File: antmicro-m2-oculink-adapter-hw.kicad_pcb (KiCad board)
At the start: 4 copper layers, 22 x 80 mm, 24 parts, among them J1 PCB-Edge_M.2_Key-M, J2 OCuLink_x4_Amphenol_G14A42121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

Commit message: [#81131] Clean drc
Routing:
- net /~{PERST}: track 58.2 -> 60.8 mm
- added copper zone on F.Cu, net Net-(J2-V_{ACT}_TX_3V3)
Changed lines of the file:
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@@
 		(tags "resistor SMD 0201")
 		(property "Reference" "R6"
-			(at 0.26 0.32 180)
+			(at -3.95 -0.85 180)
 			(layer "B.SilkS")
 			(effects
@@
 		(tags "resistor SMD 0201")
 		(property "Reference" "R9"
-			(at 1.03 -0.35 90)
+			(at 1 -0.39 90)
 			(layer "B.SilkS")
 			(effects
@@
 		(tags "resistor SMD 0201")
 		(property "Reference" "R4"
-			(at 0.25 -3.62 180)
+			(at -3.95 -1.44 180)
 			(layer "B.SilkS")
 			(effects
@@
 		(tags "resistor SMD 0201")
 		(property "Reference" "R3"
-			(at 0.5 -3.57 180)
+			(at -3.7 -1.39 180)
 			(layer "B.SilkS")
 			(effects
@@
 		(tags "resistor SMD 0201")
 		(property "Reference" "R2"
-			(at 0.7 -4.38 0)
+			(at 0.88 -4.45 0)
 			(layer "B.SilkS")
 			(effects
@@
 		(tags "resistor SMD 0201")
 		(property "Reference" "R5"
-			(at 0.5 0.35 0)
+			(at -3.71 -0.82 0)
 			(layer "B.SilkS")
 			(effects
@@
 	)
 	(segment
+		(start 147.89 97.424644)
+		(end 147.816435 97.498209)
+		(width 0.25)
+		(layer "F.Cu")
+		(net 1)
+	)
+	(segment
 		(start 138.34 122.22)
 		(end 137.74 122.22)
@@
 	)
 	(segment
-		(start 147.77 97.61)
-		(end 147.77 97.63)
-		(width 0.25)
-		(layer "F.Cu")
-		(net 1)
-	)
-	(segment
-		(start 147.767041 96.797041)
-		(end 147.77 96.8)
-		(width 0.25)
-		(layer "F.Cu")
-		(net 1)
-	)
-	(segment
 		(start 138.34 122.22)
 		(end 138.34 122.3)
@@
 	)
 	(segment
+		(start 147.767041 96.797041)
+		(end 147.89 96.92)
+		(width 0.25)
+		(layer "F.Cu")
+		(net 1)
+	)
+	(segment
 		(start 153.35 127.038482)
 		(end 153.4 127.088482)
@@
 	)
 	(segment
+		(start 147.89 96.92)
+		(end 147.89 97.424644)
+		(width 0.25)
+		(layer "F.Cu")
+		(net 1)
+	)
+	(segment
 		(start 144.27 93.713732)
 		(end 144.278134 93.721866)
@@
 	)
 	(segment
-		(start 147.77 97.462296)
-		(end 147.77 96.8)
-		(width 0.25)
-		(layer "F.Cu")
-		(net 1)
-	)
-	(segment
 		(start 145.91 127.056898)
 		(end 145.9 127.066898)
@@
 	)
 	(via
-		(at 147.77 97.61)
+		(at 147.816435 97.498209)
 		(size 0.5)
 		(drill 0.2)
@@
 	(segment
 		(start 144.51 92.75)
-		(end 144.33 92.57)
+		(end 144.36 92.75)
 		(width 0.2)
 		(layer "F.Cu")
@@
 	)
 	(segment
-		(start 144.18 92.57)
-		(end 142.7 91.09)
+		(start 142.7 91.09)
+		(end 142.7 90.34)
 		(width 0.2)
 		(layer "F.Cu")
@@
 	)
 	(segment
-		(start 142.7 91.09)
-		(end 142.7 90.34)
+		(start 142.02 89.66)
+		(end 140.75 89.66)
 		(width 0.2)
 		(layer "F.Cu")
@@
 	)
 	(segment
-		(start 144.33 92.57)
-		(end 144.18 92.57)
+		(start 144.36 92.75)
+		(end 142.7 91.09)
 		(width 0.2)
 		(layer "F.Cu")
@@
 		(net 24)
 	)
-	(segment
-		(start 142.02 89.66)
-		(end 140.75 89.66)
-		(width 0.2)
-		(layer "F.Cu")
-		(net 24)
-	)
 	(via
 		(at 145.70541 97.737935)
@@
 	)
 	(segment
-		(start 144.51 92.75)
-		(end 144.67 92.75)
-		(width 0.2)
-		(layer "B.Cu")
-		(net 24)
-	)
-	(segment
 		(start 144.71 94.44)
 		(end 144.71 95.71)
@@
 	)
 	(segment
-		(start 144.82 93.772013)
-		(end 144.71 93.882013)
+		(start 144.747 94.403)
+		(end 144.71 94.44)
 		(width 0.2)
 		(layer "B.Cu")
@@
 	)
 	(segment
-		(start 144.82 92.9)
-		(end 144.82 93.772013)
+		(start 145.732065 97.737935)
+		(end 145.70541 97.737935)
 		(width 0.2)
 		(layer "B.Cu")
@@
 	)
 	(segment
-		(start 145.732065 97.737935)
-		(end 145.70541 97.737935)
+		(start 144.51 92.75)
+		(end 144.67 92.75)
 		(width 0.2)
 		(layer "B.Cu")
@@
 	(segment
 		(start 144.67 92.75)
-		(end 144.82 92.9)
+		(end 144.747 92.827)
 		(width 0.2)
 		(layer "B.Cu")
@@
 	)
 	(segment
-		(start 144.71 93.882013)
+		(start 144.7 94.43)
 		(end 144.71 94.44)
 		(width 0.2)
@@
 	)
 	(segment
-		(start 144.7 94.43)
-		(end 144.71 94.44)
+		(start 145.74 96.74)
+		(end 145.74 97.73)
 		(width 0.2)
 		(layer "B.Cu")
@@
 	)
 	(segment
-		(start 145.74 96.74)
-		(end 145.74 97.73)
+		(start 144.747 92.827)
+		(end 144.747 94.403)
 		(width 0.2)
 		(layer "B.Cu")
@@
 	)
 	(segment
+		(start 145.27 95.37)
+		(end 145.124 95.224)
+		(width 0.2)
+		(layer "B.Cu")
+		(net 55)
+	)
+	(segment
 		(start 139.7 118.16)
 		(end 139.07 118.79)
@@
 	)
 	(segment
+		(start 145.124 95.224)
+		(end 145.124 93.130106)
+		(width 0.2)
+		(layer "B.Cu")
+		(net 55)
+	)
+	(segment
+		(start 145.124 93.130106)
+		(end 145.353999 92.900107)
+		(width 0.2)
+		(layer "B.Cu")
+		(net 55)
+	)
+	(segment
 		(start 145.353999 92.900107)
 		(end 145.336946 92.900107)
@@
 	)
 	(zone
-		(net 17)
-		(net_name "+3V3")
+		(net 57)
+		(net_name "Net-(J2-V_{ACT}_TX_3V3)")
 		(layer "F.Cu")
 		(hatch edge 0.5)
@@
 		(members "06556173-ffed-4031-9924-a6c8c4b07c0c" "16721270-387f-447d-a762-376c3936303d")
 	)
-	(group ""
-		(members "477021a0-9647-45d7-a17e-5ebdb906f6e6" "7ca616a6-a283-4b4f-b5f9-dcc5ec1ff0d3"
-			"8a60c2c5-ed15-4a37-9b29-e375b5fa27e6" "fdb1dcc9-0d94-4d31-af9d-c221d9242106"
-			"fe71ac52-9aba-4c5f-a7bf-c88477ec28cb"
-		)
-	)
 	(generated

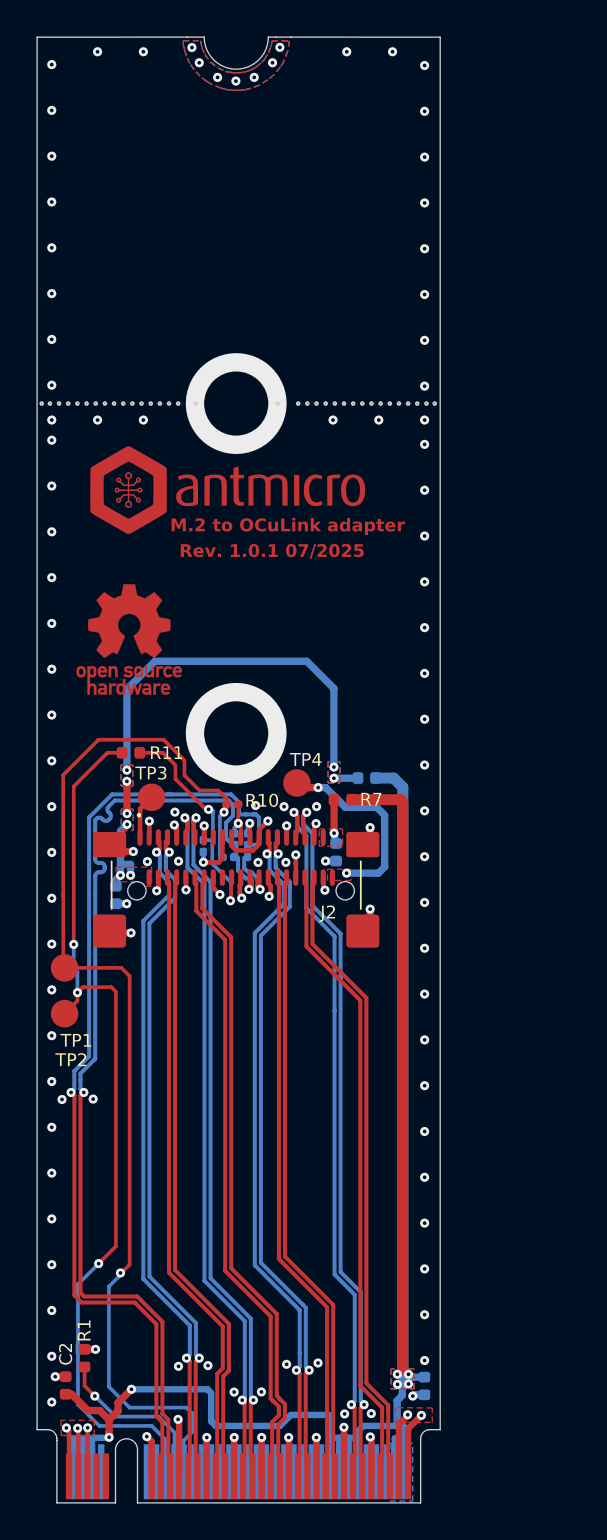
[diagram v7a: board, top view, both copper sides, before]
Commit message: [#81131] Clean-up tracks, shorten stubs, relocate R1, align silkscreen
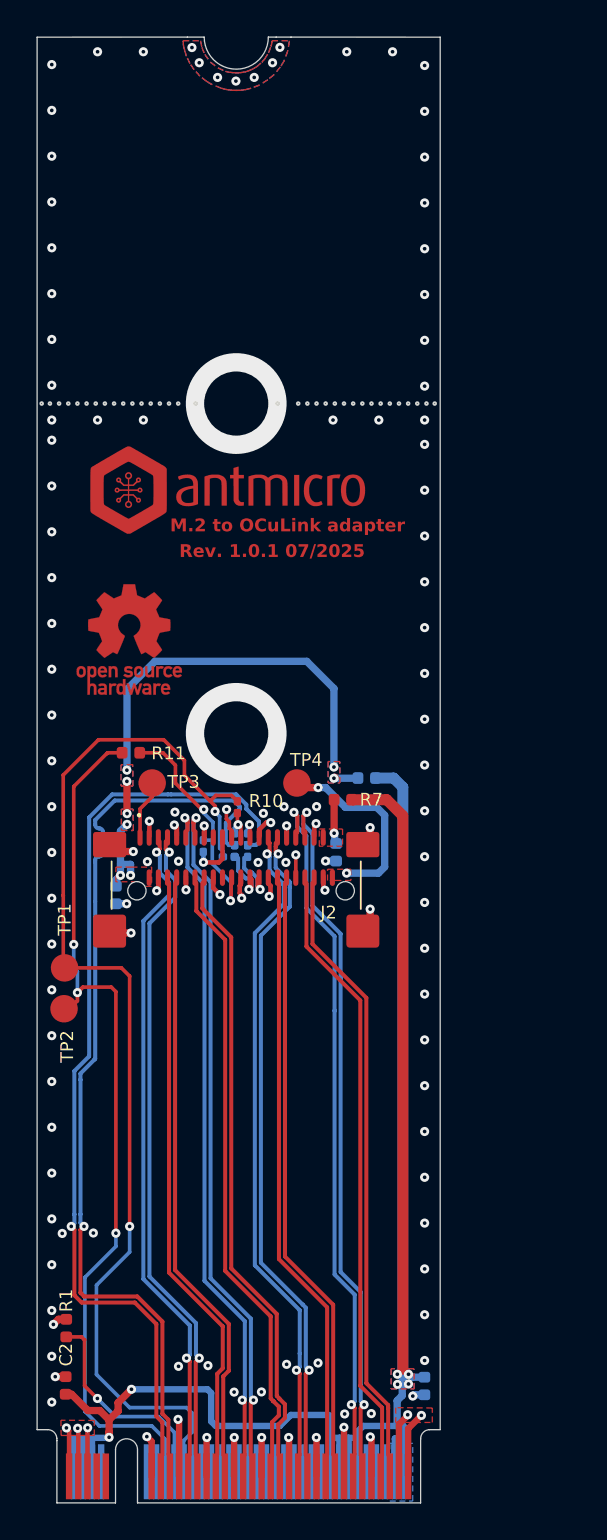
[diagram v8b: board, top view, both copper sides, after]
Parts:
- moved R1 1.92 mm to (136.7, 121.1)
- moved TP3 0.78 mm to (141.4, 91.3)
- moved R10 0.31 mm to (146.1, 92.6), turned to -90 degrees
- moved TP2 0.27 mm to (136.6, 103.6)
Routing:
- net Net-(J1-CLKREQ#): track 9.13 -> 11.7 mm
- net /~{PERST}: track 60.8 -> 62.1 mm
- net Net-(J2-5V-PadA21): track 12.7 -> 13.8 mm
- net GND: track 56.6 -> 56.0 mm, vias 132 -> 133
